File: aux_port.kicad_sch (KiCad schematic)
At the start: 32 parts, among them IC1 ECP5-BGA256, J5 MEZZANINE, U11 USB3343-CP, U12 FUSB302B, U14 DPO2036

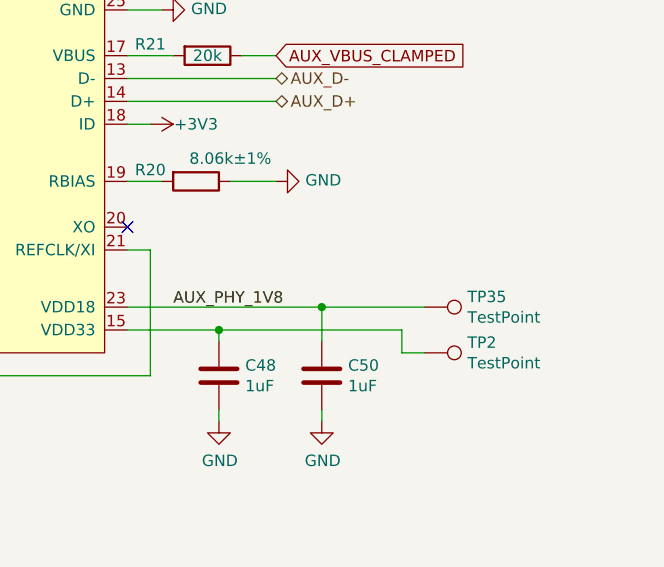
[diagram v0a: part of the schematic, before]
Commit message: Connect PHY pin 15 VDD33 to +3V3
This bypasses the PHY's internal 3.3 V regulator and ties it to the
board's +3V3 net, taking advantage of the superior decoupling of +3V3.
VDD33 test points are retained for test jig compatibility and in case
this change is reverted, but they could be removed in the future.
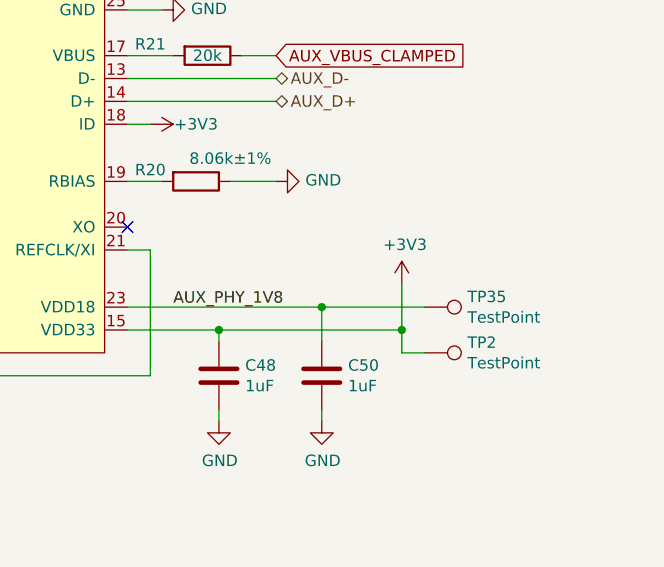
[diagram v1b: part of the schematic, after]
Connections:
- net +3V3: now also C48.1, TP2.1, U11.15 (VDD33)
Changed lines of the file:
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@@
   (junction (at 240.665 30.48) (diameter 0) (color 0 0 0 0)
+  )
+  (junction (at 257.81 149.86) (diameter 0) (color 0 0 0 0)
   )
   (junction (at 181.61 52.705) (diameter 0) (color 0 0 0 0)
@@
   )
   (wire (pts (xy 194.31 139.7) (xy 191.77 139.7))
+    (stroke (width 0) (type default) (color 0 0 0 0))
+  )
+  (wire (pts (xy 257.81 149.86) (xy 257.81 144.78))
     (stroke (width 0) (type default) (color 0 0 0 0))
   )
@@
       (effects (font (size 1.27 1.27)) hide)
     )
+    (pin "1")
+  )
+  (symbol (lib_id "power:+3V3") (at 257.81 144.78 0) (unit 1)
+    (in_bom yes) (on_board yes)
+    (property "Reference" "#PWR068" (id 0) (at 257.81 148.59 0)
+      (effects (font (size 1.27 1.27)) hide)
+    )
+    (property "Value" "+3V3" (id 1) (at 258.1656 140.3858 0))
+    (property "Footprint" "" (id 2) (at 257.81 144.78 0)
+      (effects (font (size 1.27 1.27)) hide)
+    )
+    (property "Datasheet" "" (id 3) (at 257.81 144.78 0)
+      (effects (font (size 1.27 1.27)) hide)
+    )

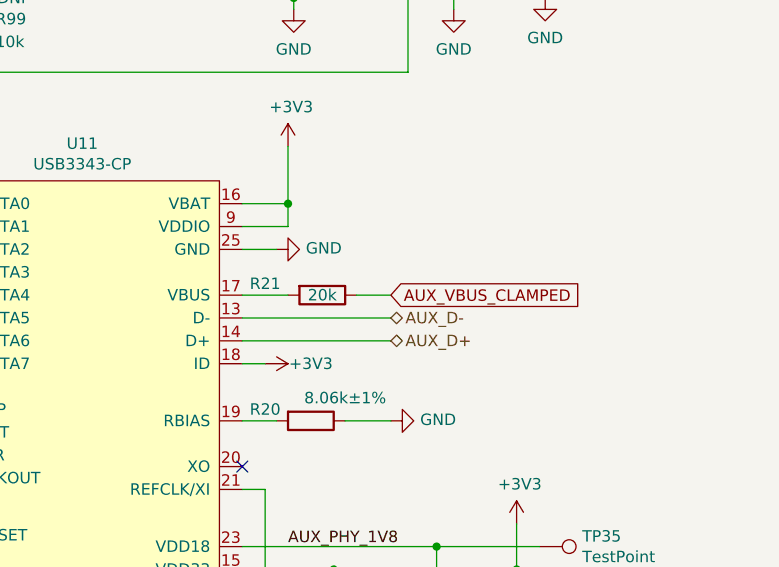
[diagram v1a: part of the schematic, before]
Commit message: Add a common-mode choke to each USB PHY
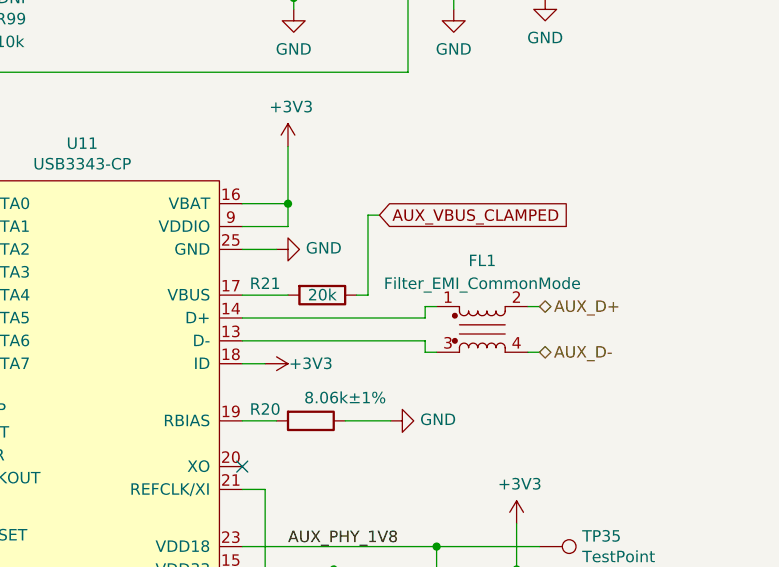
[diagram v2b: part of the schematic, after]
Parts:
- added FL1: Filter_EMI_CommonMode, cynthion:L_CommonModeChoke_Murata_DLM0NS, symbol Device:Filter_EMI_CommonMode
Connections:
- net AUX_D+: now also FL1.2; no longer U11.14 (D+)
- net AUX_D-: now also FL1.4; no longer U11.13 (D-)
- new net: FL1.3, U11.13 (D-)
- new net: FL1.1, U11.14 (D+)
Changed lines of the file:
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@@
+    (stroke (width 0) (type default) (color 0 0 0 0))
+  )
+  (wire (pts (xy 260.35 125.73) (xy 259.08 125.73))
     (stroke (width 0) (type default) (color 0 0 0 0))
   )
@@
     (stroke (width 0) (type default) (color 0 0 0 0))
   )
-  (wire (pts (xy 240.03 119.38) (xy 243.84 119.38))
-    (stroke (width 0) (type default) (color 0 0 0 0))
-  )
   (wire (pts (xy 123.19 20.32) (xy 123.19 21.59))
     (stroke (width 0) (type default) (color 0 0 0 0))
@@
     (stroke (width 0) (type default) (color 0 0 0 0))
   )
+  (wire (pts (xy 240.03 119.38) (xy 241.3 119.38))
+    (stroke (width 0) (type default) (color 0 0 0 0))
+  )
   (wire (pts (xy 201.295 30.48) (xy 201.295 24.765))
     (stroke (width 0) (type default) (color 0 0 0 0))
@@
     (stroke (width 0) (type default) (color 0 0 0 0))
   )
+  (wire (pts (xy 247.65 124.46) (xy 247.65 125.73))
+    (stroke (width 0) (type default) (color 0 0 0 0))
+  )
   (wire (pts (xy 34.29 81.28) (xy 34.29 83.82))
     (stroke (width 0) (type default) (color 0 0 0 0))
@@
     (stroke (width 0) (type default) (color 0 0 0 0))
   )
+  (wire (pts (xy 241.3 110.49) (xy 242.57 110.49))
+    (stroke (width 0) (type default) (color 0 0 0 0))
+  )
   (wire (pts (xy 120.65 138.43) (xy 118.11 138.43))
     (stroke (width 0) (type default) (color 0 0 0 0))
   )
+  (wire (pts (xy 247.65 120.65) (xy 248.92 120.65))
+    (stroke (width 0) (type default) (color 0 0 0 0))
+  )
   (wire (pts (xy 250.825 77.47) (xy 250.825 78.74))
     (stroke (width 0) (type default) (color 0 0 0 0))
@@
     (stroke (width 0) (type default) (color 0 0 0 0))
   )
-  (wire (pts (xy 227.33 124.46) (xy 243.84 124.46))
+  (wire (pts (xy 247.65 121.92) (xy 247.65 120.65))
+    (stroke (width 0) (type default) (color 0 0 0 0))
+  )
+  (wire (pts (xy 227.33 124.46) (xy 247.65 124.46))
     (stroke (width 0) (type default) (color 0 0 0 0))
   )
@@
     (stroke (width 0) (type default) (color 0 0 0 0))
   )
+  (wire (pts (xy 259.08 120.65) (xy 260.35 120.65))
+    (stroke (width 0) (type default) (color 0 0 0 0))
+  )
   (bus (pts (xy 165.1 135.89) (xy 165.1 137.16))
     (stroke (width 0) (type default) (color 0 0 0 0))
@@
     (stroke (width 0) (type default) (color 0 0 0 0))
   )
-  (wire (pts (xy 227.33 121.92) (xy 243.84 121.92))
+  (wire (pts (xy 227.33 121.92) (xy 247.65 121.92))
     (stroke (width 0) (type default) (color 0 0 0 0))
   )
@@
     (stroke (width 0) (type default) (color 0 0 0 0))
   )
+  (wire (pts (xy 247.65 125.73) (xy 248.92 125.73))
+    (stroke (width 0) (type default) (color 0 0 0 0))
+  )
   (wire (pts (xy 260.985 72.39) (xy 273.685 72.39))
     (stroke (width 0) (type default) (color 0 0 0 0))
@@
   )
   (wire (pts (xy 82.55 113.03) (xy 52.07 113.03))
+    (stroke (width 0) (type default) (color 0 0 0 0))
+  )
+  (wire (pts (xy 241.3 119.38) (xy 241.3 110.49))
     (stroke (width 0) (type default) (color 0 0 0 0))
   )
@@
     (effects (font (size 1.27 1.27)) (justify right bottom))
   )
-  (global_label "AUX_VBUS_CLAMPED" (shape input) (at 243.84 119.38 0) (fields_autoplaced)
+  (global_label "AUX_VBUS_CLAMPED" (shape input) (at 242.57 110.49 0) (fields_autoplaced)
     (effects (font (size 1.27 1.27)) (justify left))
-    (property "Intersheet References" "${INTERSHEET_REFS}" (id 0) (at 265.1537 119.3006 0)
+    (property "Intersheet References" "${INTERSHEET_REFS}" (id 0) (at 263.8837 110.4106 0)
       (effects (font (size 1.27 1.27)) (justify left) hide)
     )
@@
     )
   )
-  (hierarchical_label "AUX_D-" (shape bidirectional) (at 243.84 121.92 0)
+  (hierarchical_label "AUX_D-" (shape bidirectional) (at 260.35 125.73 0)
     (effects (font (size 1.27 1.27)) (justify left))
   )
@@
     (effects (font (size 1.27 1.27)) (justify left))
   )
-  (hierarchical_label "AUX_D+" (shape bidirectional) (at 243.84 124.46 0)
+  (hierarchical_label "AUX_D+" (shape bidirectional) (at 260.35 120.65 0)
     (effects (font (size 1.27 1.27)) (justify left))
   )
@@
     (pin "1")
   )
+  (symbol (lib_id "Device:Filter_EMI_CommonMode") (at 254 123.19 0) (unit 1)
+    (in_bom yes) (on_board yes)
+    (property "Reference" "FL1" (id 0) (at 254 115.57 0))
+    (property "Value" "Filter_EMI_CommonMode" (id 1) (at 254 118.1069 0))
+    (property "Footprint" "cynthion:L_CommonModeChoke_Murata_DLM0NS" (id 2) (at 254 122.174 0)
+      (effects (font (size 1.27 1.27)) hide)
+    )
+    (property "Datasheet" "https://www.murata.com/en-global/products/productdata/8799424610334/EFLD0009.pdf" (id 3) (at 254 122.174 0)
+      (effects (font (size 1.27 1.27)) hide)
+    )
+    (property "Description" "CMC 100MA 2LN 90 OHM SMD" (id 4) (at 254 123.19 0)
+      (effects (font (size 1.27 1.27)) hide)
+    )
+    (property "Manufacturer" "Murata" (id 5) (at 254 123.19 0)
+      (effects (font (size 1.27 1.27)) hide)
+    )
+    (property "Part Number" "DLM0NSN900HY2D" (id 6) (at 254 123.19 0)
+      (effects (font (size 1.27 1.27)) hide)
+    )
+    (pin "1")
+    (pin "2")
+    (pin "3")
+    (pin "4")
+  )
   (symbol (lib_id "power:GND") (at 217.805 40.64 0) (mirror y) (unit 1)

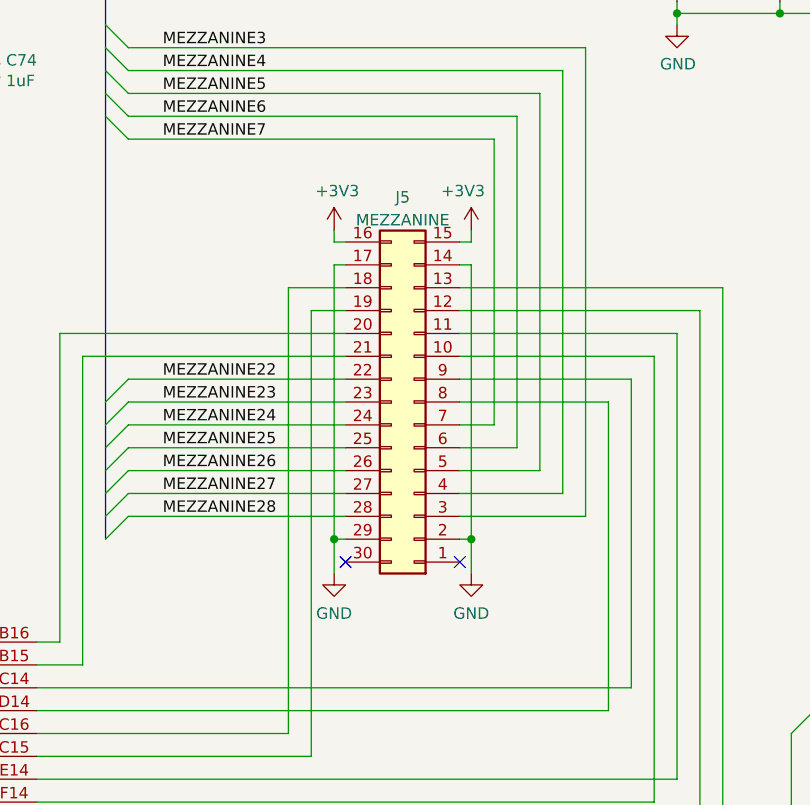
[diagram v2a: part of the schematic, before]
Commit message: Ground mezzanine connector J5 mounting pin
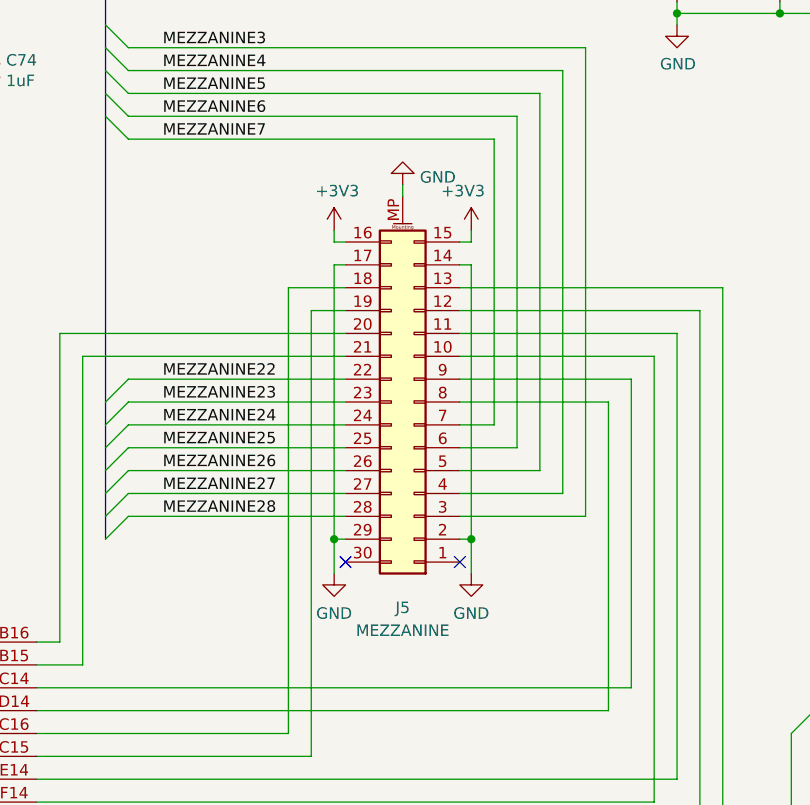
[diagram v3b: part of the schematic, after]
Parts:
- J5: symbol Connector_Generic:Conn_02x15_Counter_Clockwise -> Connector_Generic_MountingPin:Conn_02x15_Counter_Clockwise_MountingPin
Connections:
- net GND: now also J5.MP (MountPin)
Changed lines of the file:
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@@
+    (stroke (width 0) (type default) (color 0 0 0 0))
+  )
+  (wire (pts (xy 92.71 50.8) (xy 92.71 49.53))
     (stroke (width 0) (type default) (color 0 0 0 0))
   )
@@
     (pin "2")
   )
+  (symbol (lib_id "power:GND") (at 92.71 49.53 180) (unit 1)
+    (in_bom yes) (on_board yes) (fields_autoplaced)
+    (property "Reference" "#PWR0246" (id 0) (at 92.71 43.18 0)
+      (effects (font (size 1.27 1.27)) hide)
+    )
+    (property "Value" "GND" (id 1) (at 94.615 48.6938 0)
+      (effects (font (size 1.27 1.27)) (justify right))
+    )
+    (property "Footprint" "" (id 2) (at 92.71 49.53 0)
+      (effects (font (size 1.27 1.27)) hide)
+    )
+    (property "Datasheet" "" (id 3) (at 92.71 49.53 0)
+      (effects (font (size 1.27 1.27)) hide)
+    )
+    (pin "1")
+  )
   (symbol (lib_id "power:+3V3") (at 198.12 84.455 0) (unit 1)
     (in_bom yes) (on_board yes)
@@
     (pin "1")
   )
-  (symbol (lib_id "Connector_Generic:Conn_02x15_Counter_Clockwise") (at 93.98 73.66 180) (unit 1)
-    (in_bom yes) (on_board yes) (fields_autoplaced)
-    (property "Reference" "J5" (id 0) (at 92.71 50.9102 0))
-    (property "Value" "MEZZANINE" (id 1) (at 92.71 53.4471 0))
+  (symbol (lib_id "Connector_Generic_MountingPin:Conn_02x15_Counter_Clockwise_MountingPin") (at 93.98 73.66 180) (unit 1)
+    (in_bom yes) (on_board yes)
+    (property "Reference" "J5" (id 0) (at 92.71 96.52 0))
+    (property "Value" "MEZZANINE" (id 1) (at 92.71 99.0569 0))
     (property "Footprint" "cynthion:Amphenol_10132798-03" (id 2) (at 93.98 73.66 0)
       (effects (font (size 1.27 1.27)) hide)
@@
     (pin "8")
     (pin "9")
+    (pin "MP")
   )
   (symbol (lib_id "usb:DPO2036") (at 233.045 73.66 0) (mirror y) (unit 1)
